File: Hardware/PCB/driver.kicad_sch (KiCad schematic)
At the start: 182 parts, among them J11 Hr_Ten, J12 Hr_One, J13 Min_Dec, J14 Min_Ten, J15 Min_One, J16 Sec_Dec, J17 Sec_Ten, J18 Sec_One, Q10 MPSA42, Q11 MPSA42, Q12 MPSA42, Q13 MPSA42, Q14 MPSA42, Q15 MPSA42, Q16 MPSA42, Q17 MPSA42, Q18 MPSA42, Q19 MPSA42, Q20 MPSA42, Q21 MPSA42, Q22 MPSA42, Q23 MPSA42, Q24 MPSA42, Q25 MPSA42, Q26 MPSA42, Q27 MPSA42, Q28 MPSA42, Q29 MPSA42, Q30 MPSA42, Q31 MPSA42, Q32 MPSA42, Q33 MPSA42, Q34 MPSA42, Q35 MPSA42, Q36 MPSA42, Q37 MPSA42, Q38 MPSA42, Q39 MPSA42, Q40 MPSA42, Q41 MPSA42, Q42 MPSA42, Q43 MPSA42, Q44 MPSA42, Q45 MPSA42, Q46 MPSA42, Q47 MPSA42, Q48 MPSA42, Q49 MPSA42, Q50 MPSA42, Q51 MPSA42, Q52 MPSA42, Q53 MPSA42, Q54 MPSA42, Q55 MPSA42, Q56 MPSA42, Q57 MPSA42, Q58 MPSA42, Q59 MPSA42, Q6 MPSA42, Q60 MPSA42, Q61 MPSA42, Q62 MPSA42, Q63 MPSA42, Q64 MPSA42, Q65 MPSA42, Q66 MPSA42, Q67 MPSA42, Q68 MPSA42, Q69 MPSA42, Q7 MPSA42, Q70 MPSA42, Q71 MPSA92, Q72 MPSA92, Q73 MPSA42, Q74 MPSA92, Q75 MPSA42, Q76 MPSA92, Q77 MPSA42, Q78 MPSA92, Q79 MPSA42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

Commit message: schematic update
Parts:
- removed J13: Min_Dec, symbol Connector_Generic:Conn_01x04
- added J21: Sec_Dec, symbol Connector_Generic:Conn_01x04
- added Q81, Q83: MPSA92, Package_TO_SOT_THT:TO-92, symbol Transistor_BJT:MPSA92
- added Q82, Q84: MPSA42, Package_TO_SOT_THT:TO-92, symbol Transistor_BJT:MPSA42
- added R103, R19, R39, R59, R63, R83: 15k, symbol Device:R
- added R104, R106, R109, R111: 150k, symbol Device:R
- added R105, R110: 220k, symbol Device:R
- added R107, R112: 100k, symbol Device:R
- added R108, R113: 1k, symbol Device:R
- renumbered C24 to C10, C25 to C11, C26 to C12, C27 to C13, C28 to C14, C29 to C15, C30 to C16, C23 to C9, J18 to J14, J17 to J15, J15 to J16, J14 to J17, J12 to J18, J11 to J19, J16 to J20, Q9 to Q10, Q10 to Q11, Q11 to Q12, Q12 to Q13, Q13 to Q14, Q14 to Q15, Q15 to Q16, Q16 to Q17, Q17 to Q18, Q18 to Q19, Q19 to Q20, Q20 to Q21, Q21 to Q22, Q72 to Q23, Q73 to Q24, Q22 to Q25, Q23 to Q26, Q24 to Q27, Q25 to Q28, Q26 to Q29, Q27 to Q30, Q28 to Q31, Q29 to Q32, Q30 to Q33, Q31 to Q34, Q32 to Q35, Q33 to Q36, Q34 to Q37, Q35 to Q38, Q36 to Q39, Q37 to Q40, Q74 to Q41, Q75 to Q42, Q76 to Q43, Q77 to Q44, Q38 to Q45, Q39 to Q46, Q40 to Q47, Q41 to Q48, Q42 to Q49, Q71 to Q5, Q43 to Q50, Q44 to Q51, Q45 to Q52, Q46 to Q53, Q47 to Q54, Q48 to Q55, Q49 to Q56, Q50 to Q57, Q51 to Q58, Q52 to Q59, Q70 to Q6, Q53 to Q60, Q78 to Q61, Q79 to Q62, Q80 to Q63, Q54 to Q64, Q55 to Q65, Q56 to Q66, Q57 to Q67, Q58 to Q68, Q59 to Q69, Q6 to Q7, Q60 to Q70, Q61 to Q71, Q62 to Q72, Q63 to Q73, Q64 to Q74, Q65 to Q75, Q66 to Q76, Q67 to Q77, Q68 to Q78, Q69 to Q79, Q7 to Q8, Q81 to Q80, Q8 to Q9, R88 to R100, R89 to R101, R107 to R102, R91 to R16, R92 to R17, R90 to R18, R26 to R20, R27 to R21, R28 to R22, R29 to R23, R30 to R24, R31 to R25, R32 to R26, R33 to R27, R34 to R28, R35 to R29, R36 to R30, R37 to R31, R38 to R32, R39 to R33, R40 to R34, R41 to R35, R93 to R36, R94 to R37, R95 to R38, R96 to R40, R42 to R41, R43 to R42, R44 to R43, R45 to R44, R46 to R45, R47 to R46, R48 to R47, R49 to R48, R50 to R49, R51 to R50, R52 to R51, R53 to R52, R54 to R53, R55 to R54, R56 to R55, R57 to R56, R97 to R57, R98 to R58, R99 to R60, R100 to R61, R101 to R62, R58 to R64, R59 to R65, R60 to R66, R61 to R67, R62 to R68, R63 to R69, R64 to R70, R65 to R71, R66 to R72, R67 to R73, R68 to R74, R69 to R75, R70 to R76, R71 to R77, R72 to R78, R73 to R79, R102 to R80, R103 to R81, R104 to R82, R105 to R84, R106 to R85, R74 to R86, R75 to R87, R76 to R88, R77 to R89, R78 to R90, R79 to R91, R80 to R92, R81 to R93, R82 to R94, R83 to R95, R84 to R96, R85 to R97, R86 to R98, R87 to R99, U14 to U15, U15 to U16, U16 to U17, U17 to U18, U18 to U19, U19 to U20, U20 to U21, U21 to U22
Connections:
- net +180V: now also Q81.1 (E), Q83.1 (E), R105.2, R110.2; no longer J20.4 (Pin_4)
- net Bit20: now also R104.2, R109.2; no longer J20.1 (Pin_1)
- net Bit21: now also R106.2, R111.2; no longer J20.2 (Pin_2)
- net GND: now also Q82.1 (E), Q84.1 (E)
- net at Q41.3 (C): now also R59.2; no longer J16.12 (Pin_12)
- net at J19.12 (Pin_12): now also R103.1; no longer Q63.3 (C)
- net at J15.12 (Pin_12): now also R39.1; no longer Q23.3 (C)
- net at Q5.3 (C): now also R19.2; no longer J14.12 (Pin_12)
- net at J17.12 (Pin_12): now also R63.1; no longer Q43.3 (C)
- net at J18.12 (Pin_12): now also R83.1; no longer Q61.3 (C)
- new net: Q23.3 (C), R39.2
- new net: Q61.3 (C), R83.2
- new net: Q81.2 (B), R105.1, R107.1
- new net: Q82.3 (C), R107.2
- new net: Q83.2 (B), R110.1, R112.1
- new net: J16.12 (Pin_12), R59.1
- new net: Q63.3 (C), R103.2
- new net: Q84.3 (C), R112.2
- new net: Q43.3 (C), R63.2
- new net: Q84.2 (B), R113.1
- new net: J21.1 (Pin_1), R109.1
- new net: J21.2 (Pin_2), R111.1
- new net: J21.4 (Pin_4), Q83.3 (C)
- new net: J20.4 (Pin_4), Q81.3 (C)
- new net: J14.12 (Pin_12), R19.1
- new net: Q82.2 (B), R108.1
- new net: J20.1 (Pin_1), R104.1
- new net: J20.2 (Pin_2), R106.1
- new net A6: R108.2
- new net A7: R113.2
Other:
- moved on the sheet: J16, J17, J18, J19, J20, Q41, Q42, Q43, Q44, Q61, Q62, Q63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

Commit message: Hardware Update Schematic Done Placement started
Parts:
- C301: renamed from C9; footprint (none) -> Capacitor_THT:C_Disc_D3.0mm_W1.6mm_P2.50mm
- C302: renamed from C10; footprint (none) -> Capacitor_THT:C_Disc_D3.0mm_W1.6mm_P2.50mm
- C303: renamed from C11; footprint (none) -> Capacitor_THT:C_Disc_D3.0mm_W1.6mm_P2.50mm
- C304: renamed from C12; footprint (none) -> Capacitor_THT:C_Disc_D3.0mm_W1.6mm_P2.50mm
- C305: renamed from C13; footprint (none) -> Capacitor_THT:C_Disc_D3.0mm_W1.6mm_P2.50mm
- C306: renamed from C14; footprint (none) -> Capacitor_THT:C_Disc_D3.0mm_W1.6mm_P2.50mm
- C307: renamed from C15; footprint (none) -> Capacitor_THT:C_Disc_D3.0mm_W1.6mm_P2.50mm
- C308: renamed from C16; footprint (none) -> Capacitor_THT:C_Disc_D3.0mm_W1.6mm_P2.50mm
- J301: renamed from J14; footprint (none) -> Connector_PinHeader_2.54mm:PinHeader_1x12_P2.54mm_Vertical
- J302: renamed from J15; footprint (none) -> Connector_PinHeader_2.54mm:PinHeader_1x12_P2.54mm_Vertical
- J303: renamed from J16; footprint (none) -> Connector_PinHeader_2.54mm:PinHeader_1x12_P2.54mm_Vertical
- J304: renamed from J17; footprint (none) -> Connector_PinHeader_2.54mm:PinHeader_1x12_P2.54mm_Vertical
- J305: renamed from J18; footprint (none) -> Connector_PinHeader_2.54mm:PinHeader_1x12_P2.54mm_Vertical
- J306: renamed from J19; footprint (none) -> Connector_PinHeader_2.54mm:PinHeader_1x12_P2.54mm_Vertical
- J307: renamed from J20; footprint (none) -> Connector_PinHeader_2.54mm:PinHeader_1x04_P2.54mm_Vertical
- J308: renamed from J21; footprint (none) -> Connector_PinHeader_2.54mm:PinHeader_1x04_P2.54mm_Vertical
- R301: renamed from R16; footprint (none) -> Resistor_THT:R_Axial_DIN0207_L6.3mm_D2.5mm_P2.54mm_Vertical
- R302: renamed from R17; footprint (none) -> Resistor_THT:R_Axial_DIN0207_L6.3mm_D2.5mm_P2.54mm_Vertical
- R303: renamed from R18; footprint (none) -> Resistor_THT:R_Axial_DIN0207_L6.3mm_D2.5mm_P2.54mm_Vertical
- R304: renamed from R19; footprint (none) -> Resistor_THT:R_Axial_DIN0207_L6.3mm_D2.5mm_P2.54mm_Vertical
- R305: renamed from R20; footprint (none) -> Resistor_THT:R_Axial_DIN0207_L6.3mm_D2.5mm_P2.54mm_Vertical
- R306: renamed from R21; footprint (none) -> Resistor_THT:R_Axial_DIN0207_L6.3mm_D2.5mm_P2.54mm_Vertical
- R307: renamed from R22; footprint (none) -> Resistor_THT:R_Axial_DIN0207_L6.3mm_D2.5mm_P2.54mm_Vertical
- R308: renamed from R23; footprint (none) -> Resistor_THT:R_Axial_DIN0207_L6.3mm_D2.5mm_P2.54mm_Vertical
- R309: renamed from R24; footprint (none) -> Resistor_THT:R_Axial_DIN0207_L6.3mm_D2.5mm_P2.54mm_Vertical
- R310: renamed from R25; footprint (none) -> Resistor_THT:R_Axial_DIN0207_L6.3mm_D2.5mm_P2.54mm_Vertical
- R311: renamed from R26; footprint (none) -> Resistor_THT:R_Axial_DIN0207_L6.3mm_D2.5mm_P2.54mm_Vertical
- R312: renamed from R27; footprint (none) -> Resistor_THT:R_Axial_DIN0207_L6.3mm_D2.5mm_P2.54mm_Vertical
- R313: renamed from R28; footprint (none) -> Resistor_THT:R_Axial_DIN0207_L6.3mm_D2.5mm_P2.54mm_Vertical
- R314: renamed from R29; footprint (none) -> Resistor_THT:R_Axial_DIN0207_L6.3mm_D2.5mm_P2.54mm_Vertical
- R315: renamed from R30; footprint (none) -> Resistor_THT:R_Axial_DIN0207_L6.3mm_D2.5mm_P2.54mm_Vertical
- R316: renamed from R31; footprint (none) -> Resistor_THT:R_Axial_DIN0207_L6.3mm_D2.5mm_P2.54mm_Vertical
- R317: renamed from R32; footprint (none) -> Resistor_THT:R_Axial_DIN0207_L6.3mm_D2.5mm_P2.54mm_Vertical
- R318: renamed from R33; footprint (none) -> Resistor_THT:R_Axial_DIN0207_L6.3mm_D2.5mm_P2.54mm_Vertical
- R319: renamed from R34; footprint (none) -> Resistor_THT:R_Axial_DIN0207_L6.3mm_D2.5mm_P2.54mm_Vertical
- R320: renamed from R35; footprint (none) -> Resistor_THT:R_Axial_DIN0207_L6.3mm_D2.5mm_P2.54mm_Vertical
- R321: renamed from R36; footprint (none) -> Resistor_THT:R_Axial_DIN0207_L6.3mm_D2.5mm_P2.54mm_Vertical
- R322: renamed from R37; footprint (none) -> Resistor_THT:R_Axial_DIN0207_L6.3mm_D2.5mm_P2.54mm_Vertical
- R323: renamed from R38; footprint (none) -> Resistor_THT:R_Axial_DIN0207_L6.3mm_D2.5mm_P2.54mm_Vertical
- R324: renamed from R39; footprint (none) -> Resistor_THT:R_Axial_DIN0207_L6.3mm_D2.5mm_P2.54mm_Vertical
- R325: renamed from R40; footprint (none) -> Resistor_THT:R_Axial_DIN0207_L6.3mm_D2.5mm_P2.54mm_Vertical
- R326: renamed from R41; footprint (none) -> Resistor_THT:R_Axial_DIN0207_L6.3mm_D2.5mm_P2.54mm_Vertical
- R327: renamed from R42; footprint (none) -> Resistor_THT:R_Axial_DIN0207_L6.3mm_D2.5mm_P2.54mm_Vertical
- R328: renamed from R43; footprint (none) -> Resistor_THT:R_Axial_DIN0207_L6.3mm_D2.5mm_P2.54mm_Vertical
- R329: renamed from R44; footprint (none) -> Resistor_THT:R_Axial_DIN0207_L6.3mm_D2.5mm_P2.54mm_Vertical
- R330: renamed from R45; footprint (none) -> Resistor_THT:R_Axial_DIN0207_L6.3mm_D2.5mm_P2.54mm_Vertical
- R331: renamed from R46; footprint (none) -> Resistor_THT:R_Axial_DIN0207_L6.3mm_D2.5mm_P2.54mm_Vertical
- R332: renamed from R47; footprint (none) -> Resistor_THT:R_Axial_DIN0207_L6.3mm_D2.5mm_P2.54mm_Vertical
- R333: renamed from R48; footprint (none) -> Resistor_THT:R_Axial_DIN0207_L6.3mm_D2.5mm_P2.54mm_Vertical
- R334: renamed from R49; footprint (none) -> Resistor_THT:R_Axial_DIN0207_L6.3mm_D2.5mm_P2.54mm_Vertical
- R335: renamed from R50; footprint (none) -> Resistor_THT:R_Axial_DIN0207_L6.3mm_D2.5mm_P2.54mm_Vertical
- R336: renamed from R51; footprint (none) -> Resistor_THT:R_Axial_DIN0207_L6.3mm_D2.5mm_P2.54mm_Vertical
- R337: renamed from R52; footprint (none) -> Resistor_THT:R_Axial_DIN0207_L6.3mm_D2.5mm_P2.54mm_Vertical
- R338: renamed from R53; footprint (none) -> Resistor_THT:R_Axial_DIN0207_L6.3mm_D2.5mm_P2.54mm_Vertical
- R339: renamed from R54; footprint (none) -> Resistor_THT:R_Axial_DIN0207_L6.3mm_D2.5mm_P2.54mm_Vertical
- R340: renamed from R55; footprint (none) -> Resistor_THT:R_Axial_DIN0207_L6.3mm_D2.5mm_P2.54mm_Vertical
- R341: renamed from R56; footprint (none) -> Resistor_THT:R_Axial_DIN0207_L6.3mm_D2.5mm_P2.54mm_Vertical
- R342: renamed from R57; footprint (none) -> Resistor_THT:R_Axial_DIN0207_L6.3mm_D2.5mm_P2.54mm_Vertical
- R343: renamed from R58; footprint (none) -> Resistor_THT:R_Axial_DIN0207_L6.3mm_D2.5mm_P2.54mm_Vertical
- R344: renamed from R59; footprint (none) -> Resistor_THT:R_Axial_DIN0207_L6.3mm_D2.5mm_P2.54mm_Vertical
- R345: renamed from R60; footprint (none) -> Resistor_THT:R_Axial_DIN0207_L6.3mm_D2.5mm_P2.54mm_Vertical
- R346: renamed from R61; footprint (none) -> Resistor_THT:R_Axial_DIN0207_L6.3mm_D2.5mm_P2.54mm_Vertical
- R347: renamed from R62; footprint (none) -> Resistor_THT:R_Axial_DIN0207_L6.3mm_D2.5mm_P2.54mm_Vertical
- R348: renamed from R63; footprint (none) -> Resistor_THT:R_Axial_DIN0207_L6.3mm_D2.5mm_P2.54mm_Vertical
- R349: renamed from R64; footprint (none) -> Resistor_THT:R_Axial_DIN0207_L6.3mm_D2.5mm_P2.54mm_Vertical
- R350: renamed from R65; footprint (none) -> Resistor_THT:R_Axial_DIN0207_L6.3mm_D2.5mm_P2.54mm_Vertical
- R351: renamed from R66; footprint (none) -> Resistor_THT:R_Axial_DIN0207_L6.3mm_D2.5mm_P2.54mm_Vertical
- R352: renamed from R67; footprint (none) -> Resistor_THT:R_Axial_DIN0207_L6.3mm_D2.5mm_P2.54mm_Vertical
- R353: renamed from R68; footprint (none) -> Resistor_THT:R_Axial_DIN0207_L6.3mm_D2.5mm_P2.54mm_Vertical
- R354: renamed from R69; footprint (none) -> Resistor_THT:R_Axial_DIN0207_L6.3mm_D2.5mm_P2.54mm_Vertical
- R355: renamed from R70; footprint (none) -> Resistor_THT:R_Axial_DIN0207_L6.3mm_D2.5mm_P2.54mm_Vertical
- R356: renamed from R71; footprint (none) -> Resistor_THT:R_Axial_DIN0207_L6.3mm_D2.5mm_P2.54mm_Vertical
- R357: renamed from R72; footprint (none) -> Resistor_THT:R_Axial_DIN0207_L6.3mm_D2.5mm_P2.54mm_Vertical
- R358: renamed from R73; footprint (none) -> Resistor_THT:R_Axial_DIN0207_L6.3mm_D2.5mm_P2.54mm_Vertical
- R359: renamed from R74; footprint (none) -> Resistor_THT:R_Axial_DIN0207_L6.3mm_D2.5mm_P2.54mm_Vertical
- R360: renamed from R75; footprint (none) -> Resistor_THT:R_Axial_DIN0207_L6.3mm_D2.5mm_P2.54mm_Vertical
- R361: renamed from R76; footprint (none) -> Resistor_THT:R_Axial_DIN0207_L6.3mm_D2.5mm_P2.54mm_Vertical
- R362: renamed from R77; footprint (none) -> Resistor_THT:R_Axial_DIN0207_L6.3mm_D2.5mm_P2.54mm_Vertical
- R363: renamed from R78; footprint (none) -> Resistor_THT:R_Axial_DIN0207_L6.3mm_D2.5mm_P2.54mm_Vertical
- R364: renamed from R79; footprint (none) -> Resistor_THT:R_Axial_DIN0207_L6.3mm_D2.5mm_P2.54mm_Vertical
- R365: renamed from R80; footprint (none) -> Resistor_THT:R_Axial_DIN0207_L6.3mm_D2.5mm_P2.54mm_Vertical
- R366: renamed from R81; footprint (none) -> Resistor_THT:R_Axial_DIN0207_L6.3mm_D2.5mm_P2.54mm_Vertical
- R367: renamed from R82; footprint (none) -> Resistor_THT:R_Axial_DIN0207_L6.3mm_D2.5mm_P7.62mm_Horizontal
- R368: renamed from R83; footprint (none) -> Resistor_THT:R_Axial_DIN0207_L6.3mm_D2.5mm_P2.54mm_Vertical
- R369: renamed from R84; footprint (none) -> Resistor_THT:R_Axial_DIN0207_L6.3mm_D2.5mm_P2.54mm_Vertical
- R370: renamed from R85; footprint (none) -> Resistor_THT:R_Axial_DIN0207_L6.3mm_D2.5mm_P2.54mm_Vertical
- R371: renamed from R86; footprint (none) -> Resistor_THT:R_Axial_DIN0207_L6.3mm_D2.5mm_P2.54mm_Vertical
- R372: renamed from R87; footprint (none) -> Resistor_THT:R_Axial_DIN0207_L6.3mm_D2.5mm_P2.54mm_Vertical
- R373: renamed from R88; footprint (none) -> Resistor_THT:R_Axial_DIN0207_L6.3mm_D2.5mm_P2.54mm_Vertical
- R374: renamed from R89; footprint (none) -> Resistor_THT:R_Axial_DIN0207_L6.3mm_D2.5mm_P2.54mm_Vertical
- R375: renamed from R90; footprint (none) -> Resistor_THT:R_Axial_DIN0207_L6.3mm_D2.5mm_P2.54mm_Vertical
- R376: renamed from R91; footprint (none) -> Resistor_THT:R_Axial_DIN0207_L6.3mm_D2.5mm_P2.54mm_Vertical
- R377: renamed from R92; footprint (none) -> Resistor_THT:R_Axial_DIN0207_L6.3mm_D2.5mm_P2.54mm_Vertical
- R378: renamed from R93; footprint (none) -> Resistor_THT:R_Axial_DIN0207_L6.3mm_D2.5mm_P2.54mm_Vertical
- R379: renamed from R94; footprint (none) -> Resistor_THT:R_Axial_DIN0207_L6.3mm_D2.5mm_P2.54mm_Vertical
- R380: renamed from R95; footprint (none) -> Resistor_THT:R_Axial_DIN0207_L6.3mm_D2.5mm_P2.54mm_Vertical
- R381: renamed from R96; footprint (none) -> Resistor_THT:R_Axial_DIN0207_L6.3mm_D2.5mm_P2.54mm_Vertical
- R382: renamed from R97; footprint (none) -> Resistor_THT:R_Axial_DIN0207_L6.3mm_D2.5mm_P2.54mm_Vertical
- R383: renamed from R98; footprint (none) -> Resistor_THT:R_Axial_DIN0207_L6.3mm_D2.5mm_P2.54mm_Vertical
- R384: renamed from R99; footprint (none) -> Resistor_THT:R_Axial_DIN0207_L6.3mm_D2.5mm_P2.54mm_Vertical
- R385: renamed from R100; footprint (none) -> Resistor_THT:R_Axial_DIN0207_L6.3mm_D2.5mm_P2.54mm_Vertical
- R386: renamed from R101; footprint (none) -> Resistor_THT:R_Axial_DIN0207_L6.3mm_D2.5mm_P2.54mm_Vertical
- R387: renamed from R102; footprint (none) -> Resistor_THT:R_Axial_DIN0207_L6.3mm_D2.5mm_P2.54mm_Vertical
- R388: renamed from R103; footprint (none) -> Resistor_THT:R_Axial_DIN0207_L6.3mm_D2.5mm_P2.54mm_Vertical
- R389: renamed from R104; footprint (none) -> Resistor_THT:R_Axial_DIN0207_L6.3mm_D2.5mm_P2.54mm_Vertical
- R390: renamed from R105; footprint (none) -> Resistor_THT:R_Axial_DIN0207_L6.3mm_D2.5mm_P2.54mm_Vertical
- R391: renamed from R106; footprint (none) -> Resistor_THT:R_Axial_DIN0207_L6.3mm_D2.5mm_P2.54mm_Vertical
- R392: renamed from R107; footprint (none) -> Resistor_THT:R_Axial_DIN0207_L6.3mm_D2.5mm_P2.54mm_Vertical
- R393: renamed from R108; footprint (none) -> Resistor_THT:R_Axial_DIN0207_L6.3mm_D2.5mm_P7.62mm_Horizontal
- R394: renamed from R109; footprint (none) -> Resistor_THT:R_Axial_DIN0207_L6.3mm_D2.5mm_P2.54mm_Vertical
- R395: renamed from R110; footprint (none) -> Resistor_THT:R_Axial_DIN0207_L6.3mm_D2.5mm_P2.54mm_Vertical
- R396: renamed from R111; footprint (none) -> Resistor_THT:R_Axial_DIN0207_L6.3mm_D2.5mm_P2.54mm_Vertical
- R397: renamed from R112; footprint (none) -> Resistor_THT:R_Axial_DIN0207_L6.3mm_D2.5mm_P2.54mm_Vertical
- R398: renamed from R113; footprint (none) -> Resistor_THT:R_Axial_DIN0207_L6.3mm_D2.5mm_P2.54mm_Vertical
- U301: renamed from U15; footprint (none) -> Package_DIP:DIP-16_W7.62mm
- U302: renamed from U16; footprint (none) -> Package_DIP:DIP-16_W7.62mm
- U303: renamed from U17; footprint (none) -> Package_DIP:DIP-16_W7.62mm
- U304: renamed from U18; footprint (none) -> Package_DIP:DIP-16_W7.62mm
- U305: renamed from U19; footprint (none) -> Package_DIP:DIP-16_W7.62mm
- U306: renamed from U20; footprint (none) -> Package_DIP:DIP-16_W7.62mm
- U307: renamed from U21; footprint (none) -> Package_DIP:DIP-16_W7.62mm
- U308: renamed from U22; footprint (none) -> Package_DIP:DIP-16_W7.62mm
- renumbered Q5 to Q301, Q6 to Q302, Q7 to Q303, Q8 to Q304, Q9 to Q305, Q10 to Q306, Q11 to Q307, Q12 to Q308, Q13 to Q309, Q14 to Q310, Q15 to Q311, Q16 to Q312, Q17 to Q313, Q18 to Q314, Q19 to Q315, Q20 to Q316, Q21 to Q317, Q22 to Q318, Q23 to Q319, Q24 to Q320, Q25 to Q321, Q26 to Q322, Q27 to Q323, Q28 to Q324, Q29 to Q325, Q30 to Q326, Q31 to Q327, Q32 to Q328, Q33 to Q329, Q34 to Q330, Q35 to Q331, Q36 to Q332, Q37 to Q333, Q38 to Q334, Q39 to Q335, Q40 to Q336, Q41 to Q337, Q42 to Q338, Q43 to Q339, Q44 to Q340, Q45 to Q341, Q46 to Q342, Q47 to Q343, Q48 to Q344, Q49 to Q345, Q50 to Q346, Q51 to Q347, Q52 to Q348, Q53 to Q349, Q54 to Q350, Q55 to Q351, Q56 to Q352, Q57 to Q353, Q58 to Q354, Q59 to Q355, Q60 to Q356, Q61 to Q357, Q62 to Q358, Q63 to Q359, Q64 to Q360, Q65 to Q361, Q66 to Q362, Q67 to Q363, Q68 to Q364, Q69 to Q365, Q70 to Q366, Q71 to Q367, Q72 to Q368, Q73 to Q369, Q74 to Q370, Q75 to Q371, Q76 to Q372, Q77 to Q373, Q78 to Q374, Q79 to Q375, Q80 to Q376, Q81 to Q377, Q82 to Q378, Q83 to Q379, Q84 to Q380
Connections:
- net Bit20: no longer R394.2
- net Bit21: no longer R396.2
- net Bit42: now also R394.2
- net Bit43: now also R396.2

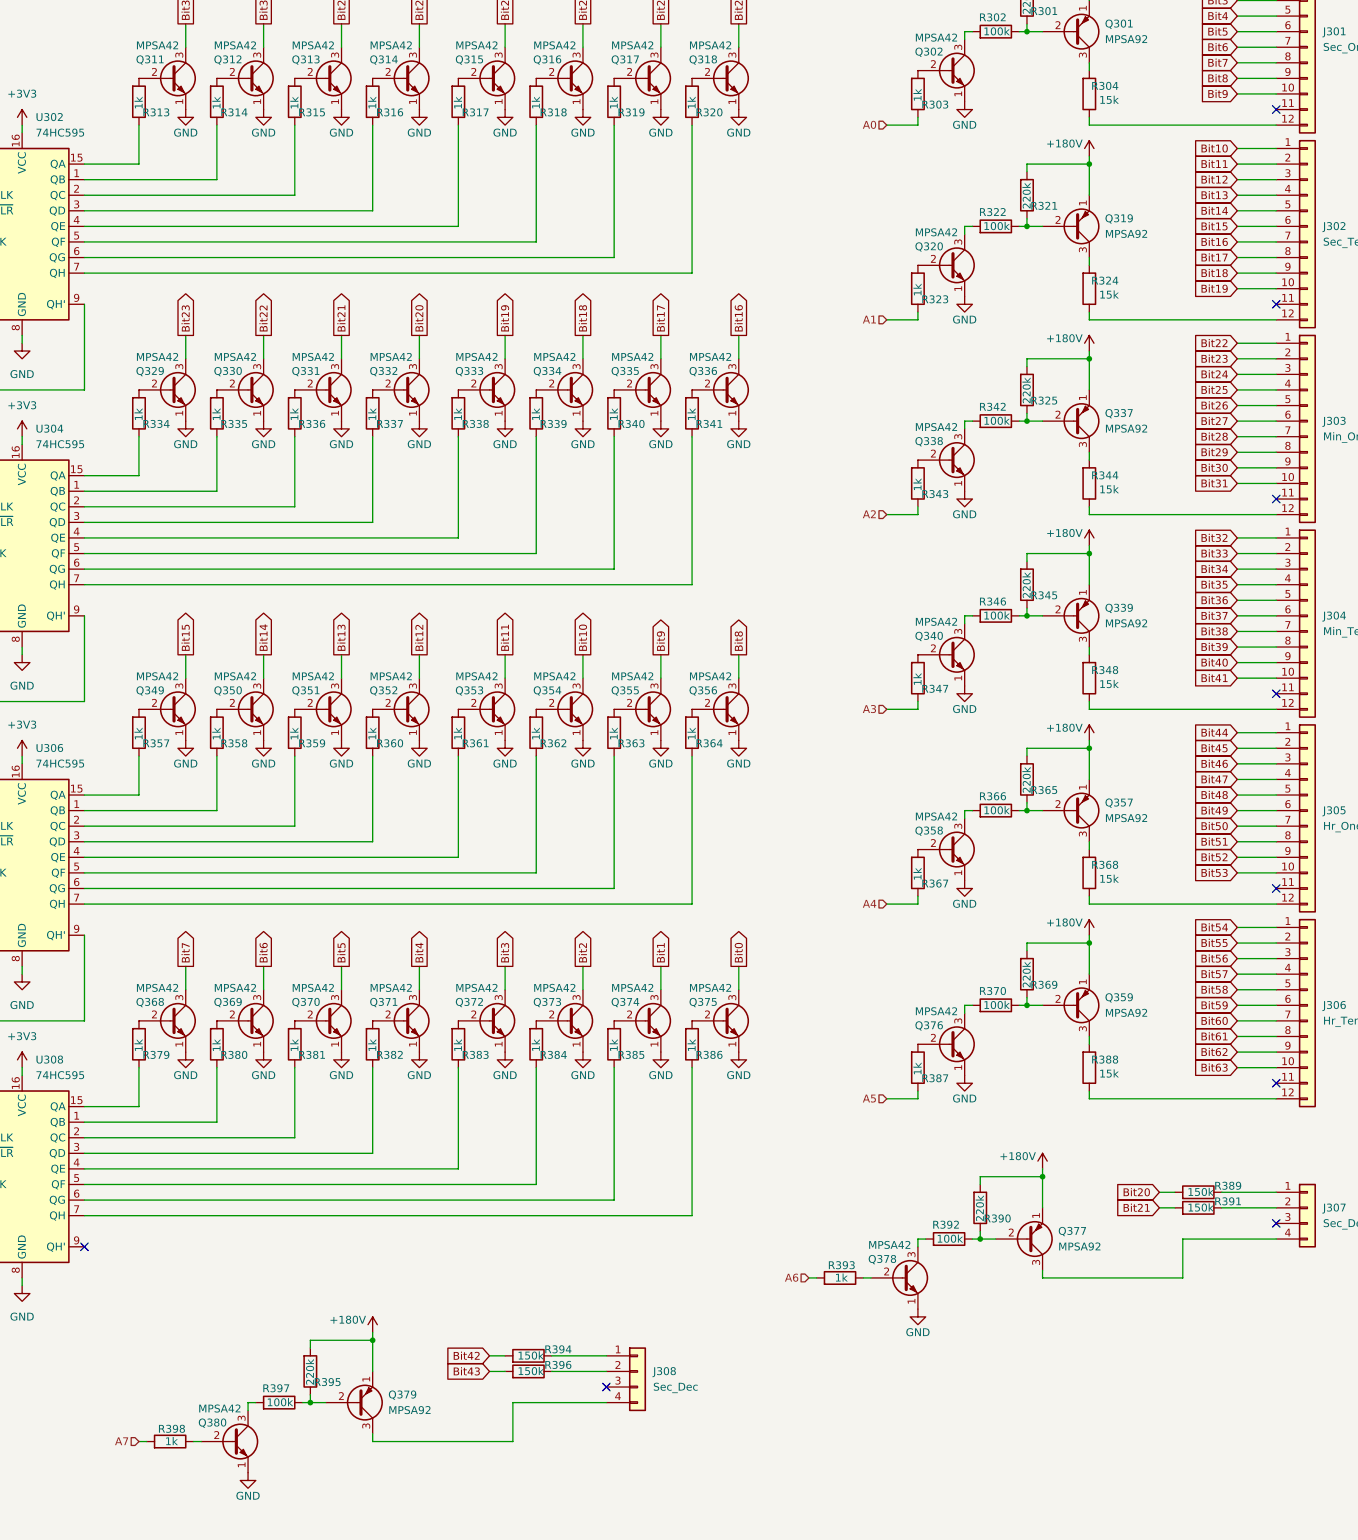
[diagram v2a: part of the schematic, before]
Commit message: PCB update finished placing and routing Cleanup Passes need to be done Silkscreen needs to be done
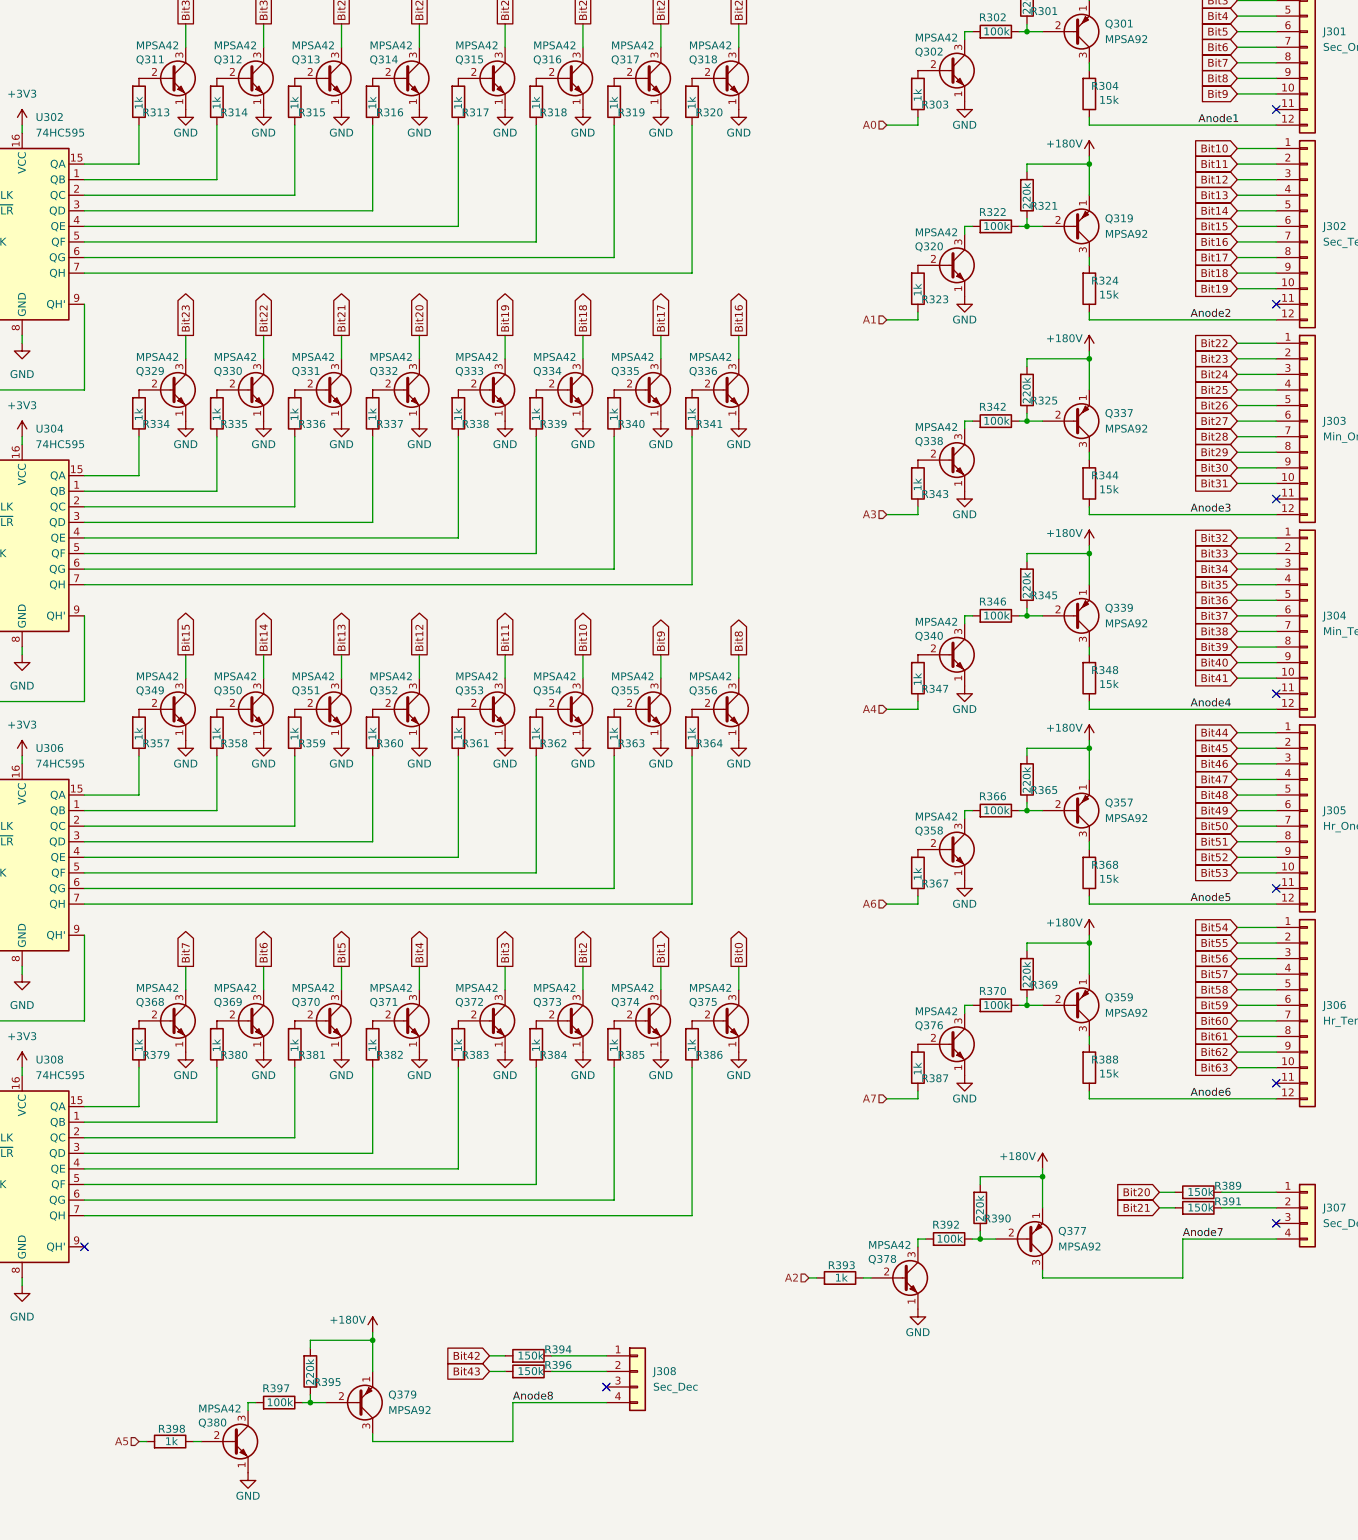
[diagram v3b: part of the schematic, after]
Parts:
- R303, R343: footprint Resistor_THT:R_Axial_DIN0207_L6.3mm_D2.5mm_P2.54mm_Vertical -> Resistor_THT:R_Axial_DIN0207_L6.3mm_D2.5mm_P7.62mm_Horizontal
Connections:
- net A2: now also R393.2; no longer R343.1
- net A3: now also R343.1; no longer R347.1
- net A4: now also R347.1; no longer R367.1
- net A5: now also R398.2; no longer R387.1
- net A6: now also R367.1; no longer R393.2
- net A7: now also R387.1; no longer R398.2
- net Anode6: now reaches J306.12 (Pin_12), R388.1
- net Anode2: now reaches J302.12 (Pin_12), R324.1
- net Anode5: now reaches J305.12 (Pin_12), R368.1
- net Anode4: now reaches J304.12 (Pin_12), R348.1
- net Anode3: now reaches J303.12 (Pin_12), R344.1
- net Anode8: now reaches J308.4 (Pin_4), Q379.3 (C)
- net Anode7: now reaches J307.4 (Pin_4), Q377.3 (C)
- net Anode1: now reaches J301.12 (Pin_12), R304.1
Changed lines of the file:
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@@
 		)
 	)
+	(label "Anode1"
+		(at 375.92 52.07 0)
+		(fields_autoplaced yes)
+		(effects
+			(font
+				(size 1.27 1.27)
+			)
+			(justify left bottom)
+		)
+	)
+	(label "Anode3"
+		(at 374.65 115.57 0)
+		(fields_autoplaced yes)
+		(effects
+			(font
+				(size 1.27 1.27)
+			)
+			(justify left bottom)
+		)
+	)
+	(label "Anode4"
+		(at 374.65 147.32 0)
+		(fields_autoplaced yes)
+		(effects
+			(font
+				(size 1.27 1.27)
+			)
+			(justify left bottom)
+		)
+	)
+	(label "Anode7"
+		(at 373.38 233.68 0)
+		(fields_autoplaced yes)
+		(effects
+			(font
+				(size 1.27 1.27)
+			)
+			(justify left bottom)
+		)
+	)
+	(label "Anode2"
+		(at 374.65 83.82 0)
+		(fields_autoplaced yes)
+		(effects
+			(font
+				(size 1.27 1.27)
+			)
+			(justify left bottom)
+		)
+	)
+	(label "Anode8"
+		(at 264.16 260.35 0)
+		(fields_autoplaced yes)
+		(effects
+			(font
+				(size 1.27 1.27)
+			)
+			(justify left bottom)
+		)
+	)
+	(label "Anode6"
+		(at 374.65 210.82 0)
+		(fields_autoplaced yes)
+		(effects
+			(font
+				(size 1.27 1.27)
+			)
+			(justify left bottom)
+		)
+	)
+	(label "Anode5"
+		(at 374.65 179.07 0)
+		(fields_autoplaced yes)
+		(effects
+			(font
+				(size 1.27 1.27)
+			)
+			(justify left bottom)
+		)
+	)
 	(global_label "Bit62"
 		(shape input)
@@
 	(hierarchical_label "A4"
 		(shape input)
-		(at 325.12 179.07 180)
+		(at 325.12 147.32 180)
 		(fields_autoplaced yes)
 		(effects
@@
 	(hierarchical_label "A3"
 		(shape input)
-		(at 325.12 147.32 180)
+		(at 325.12 115.57 180)
 		(fields_autoplaced yes)
 		(effects
@@
 	(hierarchical_label "A7"
 		(shape input)
-		(at 203.2 266.7 180)
+		(at 325.12 210.82 180)
 		(fields_autoplaced yes)
 		(effects
@@
 	(hierarchical_label "A5"
 		(shape input)
-		(at 325.12 210.82 180)
+		(at 203.2 266.7 180)
 		(fields_autoplaced yes)
 		(effects
@@
 	(hierarchical_label "A2"
 		(shape input)
-		(at 325.12 115.57 180)
+		(at 312.42 240.03 180)
 		(fields_autoplaced yes)
 		(effects
@@
 	(hierarchical_label "A6"
 		(shape input)
-		(at 312.42 240.03 180)
+		(at 325.12 179.07 180)
 		(fields_autoplaced yes)
 		(effects
@@
 			)
 		)
-		(property "Footprint" "Resistor_THT:R_Axial_DIN0207_L6.3mm_D2.5mm_P2.54mm_Vertical"
+		(property "Footprint" "Resistor_THT:R_Axial_DIN0207_L6.3mm_D2.5mm_P7.62mm_Horizontal"
 			(at 328.422 46.99 90)
 			(effects
@@
 			)
 		)
-		(property "Footprint" "Resistor_THT:R_Axial_DIN0207_L6.3mm_D2.5mm_P2.54mm_Vertical"
+		(property "Footprint" "Resistor_THT:R_Axial_DIN0207_L6.3mm_D2.5mm_P7.62mm_Horizontal"
 			(at 328.422 110.49 90)
 			(effects

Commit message: reviewed version from thebrutzler
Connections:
- net A1 is gone; now on net PWM: R323.1
- net A2 is gone; now on net PWM: R393.2
- net A3 is gone; now on net PWM: R343.1
- net A4 is gone; now on net PWM: R347.1
- net A5 is gone; now on net PWM: R398.2
- net A6 is gone; now on net PWM: R367.1
- net A7 is gone; now on net PWM: R387.1
- net A0 renamed PWM
